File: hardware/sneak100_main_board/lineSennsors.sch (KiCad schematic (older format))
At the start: 4 parts, among them J1 Conn_01x03, J2 Conn_01x03, J3 Conn_01x03, J4 Conn_01x03

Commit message: Proximity sensor first test
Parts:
- renumbered J1 to J2, J2 to J3, J3 to J4, J4 to J5
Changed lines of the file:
@@
 $EndDescr
 $Comp
-L Connector_Generic:Conn_01x03 J1
+L Connector_Generic:Conn_01x03 J2
 U 1 1 60E05377
 P 4050 2550
-F 0 "J1" H 4130 2592 50  0000 L CNN
+F 0 "J2" H 4130 2592 50  0000 L CNN
 F 1 "Conn_01x03" H 4130 2501 50  0000 L CNN
 F 2 "" H 4050 2550 50  0001 C CNN
@@
 $EndComp
 $Comp
-L Connector_Generic:Conn_01x03 J2
+L Connector_Generic:Conn_01x03 J3
 U 1 1 60E06B30
 P 4050 2950
-F 0 "J2" H 4130 2992 50  0000 L CNN
+F 0 "J3" H 4130 2992 50  0000 L CNN
 F 1 "Conn_01x03" H 4130 2901 50  0000 L CNN
 F 2 "" H 4050 2950 50  0001 C CNN
@@
 $EndComp
 $Comp
-L Connector_Generic:Conn_01x03 J3
+L Connector_Generic:Conn_01x03 J4
 U 1 1 60E07495
 P 4050 3350
-F 0 "J3" H 4130 3392 50  0000 L CNN
+F 0 "J4" H 4130 3392 50  0000 L CNN
 F 1 "Conn_01x03" H 4130 3301 50  0000 L CNN
 F 2 "" H 4050 3350 50  0001 C CNN
@@
 $EndComp
 $Comp
-L Connector_Generic:Conn_01x03 J4
+L Connector_Generic:Conn_01x03 J5
 U 1 1 60E07950
 P 4050 3750
-F 0 "J4" H 4130 3792 50  0000 L CNN
+F 0 "J5" H 4130 3792 50  0000 L CNN
 F 1 "Conn_01x03" H 4130 3701 50  0000 L CNN
 F 2 "" H 4050 3750 50  0001 C CNN
@@
 $EndComp
 $Comp
-L power:+3.3V #PWR0101
+L power:+3.3V #PWR040
 U 1 1 60E08D03
 P 3850 2550
-F 0 "#PWR0101" H 3850 2400 50  0001 C CNN
+F 0 "#PWR040" H 3850 2400 50  0001 C CNN
 F 1 "+3.3V" V 3865 2678 50  0000 L CNN
 F 2 "" H 3850 2550 50  0001 C CNN
@@
 $EndComp
 $Comp
-L power:+3.3V #PWR0102
+L power:+3.3V #PWR042
 U 1 1 60E097F5
 P 3850 2950
-F 0 "#PWR0102" H 3850 2800 50  0001 C CNN
+F 0 "#PWR042" H 3850 2800 50  0001 C CNN
 F 1 "+3.3V" V 3865 3078 50  0000 L CNN
 F 2 "" H 3850 2950 50  0001 C CNN
@@
 $EndComp
 $Comp
-L power:+3.3V #PWR0103
+L power:+3.3V #PWR044
 U 1 1 60E09BF6
 P 3850 3350
-F 0 "#PWR0103" H 3850 3200 50  0001 C CNN
+F 0 "#PWR044" H 3850 3200 50  0001 C CNN
 F 1 "+3.3V" V 3865 3478 50  0000 L CNN
 F 2 "" H 3850 3350 50  0001 C CNN
@@
 $EndComp
 $Comp
-L power:+3.3V #PWR0104
+L power:+3.3V #PWR046
 U 1 1 60E0A09F
 P 3850 3750
-F 0 "#PWR0104" H 3850 3600 50  0001 C CNN
+F 0 "#PWR046" H 3850 3600 50  0001 C CNN
 F 1 "+3.3V" V 3865 3878 50  0000 L CNN
 F 2 "" H 3850 3750 50  0001 C CNN
@@
 $EndComp
 $Comp
-L power:GND #PWR0105
+L power:GND #PWR047
 U 1 1 60E0A641
 P 3850 3850
-F 0 "#PWR0105" H 3850 3600 50  0001 C CNN
+F 0 "#PWR047" H 3850 3600 50  0001 C CNN
 F 1 "GND" V 3855 3722 50  0000 R CNN
 F 2 "" H 3850 3850 50  0001 C CNN
@@
 $EndComp
 $Comp
-L power:GND #PWR0106
+L power:GND #PWR045
 U 1 1 60E0ADFF
 P 3850 3450
-F 0 "#PWR0106" H 3850 3200 50  0001 C CNN
+F 0 "#PWR045" H 3850 3200 50  0001 C CNN
 F 1 "GND" V 3855 3322 50  0000 R CNN
 F 2 "" H 3850 3450 50  0001 C CNN
@@
 $EndComp
 $Comp
-L power:GND #PWR0107
+L power:GND #PWR043
 U 1 1 60E0B1BF
 P 3850 3050
-F 0 "#PWR0107" H 3850 2800 50  0001 C CNN
+F 0 "#PWR043" H 3850 2800 50  0001 C CNN
 F 1 "GND" V 3855 2922 50  0000 R CNN
 F 2 "" H 3850 3050 50  0001 C CNN
@@
 $EndComp
 $Comp
-L power:GND #PWR0108
+L power:GND #PWR041
 U 1 1 60E0B57F
 P 3850 2650
-F 0 "#PWR0108" H 3850 2400 50  0001 C CNN
+F 0 "#PWR041" H 3850 2400 50  0001 C CNN
 F 1 "GND" V 3855 2522 50  0000 R CNN
 F 2 "" H 3850 2650 50  0001 C CNN

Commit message: motors circuit scheme
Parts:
- J10: renamed from J5; footprint (none) -> Connector_PinHeader_2.54mm:PinHeader_1x03_P2.54mm_Vertical
- J7: renamed from J2; footprint (none) -> Connector_PinHeader_2.54mm:PinHeader_1x03_P2.54mm_Vertical
- J8: renamed from J3; footprint (none) -> Connector_PinHeader_2.54mm:PinHeader_1x03_P2.54mm_Vertical
- J9: renamed from J4; footprint (none) -> Connector_PinHeader_2.54mm:PinHeader_1x03_P2.54mm_Vertical
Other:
- note added: "QTR-1A sensors connection"
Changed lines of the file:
@@
 $EndDescr
 $Comp
-L Connector_Generic:Conn_01x03 J2
+L Connector_Generic:Conn_01x03 J7
 U 1 1 60E05377
 P 4050 2550
-F 0 "J2" H 4130 2592 50  0000 L CNN
+F 0 "J7" H 4130 2592 50  0000 L CNN
 F 1 "Conn_01x03" H 4130 2501 50  0000 L CNN
-F 2 "" H 4050 2550 50  0001 C CNN
+F 2 "Connector_PinHeader_2.54mm:PinHeader_1x03_P2.54mm_Vertical" H 4050 2550 50  0001 C CNN
 F 3 "~" H 4050 2550 50  0001 C CNN
 	1    4050 2550
@@
 $EndComp
 $Comp
-L Connector_Generic:Conn_01x03 J3
+L Connector_Generic:Conn_01x03 J8
 U 1 1 60E06B30
 P 4050 2950
-F 0 "J3" H 4130 2992 50  0000 L CNN
+F 0 "J8" H 4130 2992 50  0000 L CNN
 F 1 "Conn_01x03" H 4130 2901 50  0000 L CNN
-F 2 "" H 4050 2950 50  0001 C CNN
+F 2 "Connector_PinHeader_2.54mm:PinHeader_1x03_P2.54mm_Vertical" H 4050 2950 50  0001 C CNN
 F 3 "~" H 4050 2950 50  0001 C CNN
 	1    4050 2950
@@
 $EndComp
 $Comp
-L Connector_Generic:Conn_01x03 J4
+L Connector_Generic:Conn_01x03 J9
 U 1 1 60E07495
 P 4050 3350
-F 0 "J4" H 4130 3392 50  0000 L CNN
+F 0 "J9" H 4130 3392 50  0000 L CNN
 F 1 "Conn_01x03" H 4130 3301 50  0000 L CNN
-F 2 "" H 4050 3350 50  0001 C CNN
+F 2 "Connector_PinHeader_2.54mm:PinHeader_1x03_P2.54mm_Vertical" H 4050 3350 50  0001 C CNN
 F 3 "~" H 4050 3350 50  0001 C CNN
 	1    4050 3350
@@
 $EndComp
 $Comp
-L Connector_Generic:Conn_01x03 J5
+L Connector_Generic:Conn_01x03 J10
 U 1 1 60E07950
 P 4050 3750
-F 0 "J5" H 4130 3792 50  0000 L CNN
+F 0 "J10" H 4130 3792 50  0000 L CNN
 F 1 "Conn_01x03" H 4130 3701 50  0000 L CNN
-F 2 "" H 4050 3750 50  0001 C CNN
+F 2 "Connector_PinHeader_2.54mm:PinHeader_1x03_P2.54mm_Vertical" H 4050 3750 50  0001 C CNN
 F 3 "~" H 4050 3750 50  0001 C CNN
 	1    4050 3750
@@
 $EndComp
 $Comp
-L power:+3.3V #PWR040
+L power:+3.3V #PWR072
 U 1 1 60E08D03
 P 3850 2550
-F 0 "#PWR040" H 3850 2400 50  0001 C CNN
+F 0 "#PWR072" H 3850 2400 50  0001 C CNN
 F 1 "+3.3V" V 3865 2678 50  0000 L CNN
 F 2 "" H 3850 2550 50  0001 C CNN
@@
 $EndComp
 $Comp
-L power:+3.3V #PWR042
+L power:+3.3V #PWR074
 U 1 1 60E097F5
 P 3850 2950
-F 0 "#PWR042" H 3850 2800 50  0001 C CNN
+F 0 "#PWR074" H 3850 2800 50  0001 C CNN
 F 1 "+3.3V" V 3865 3078 50  0000 L CNN
 F 2 "" H 3850 2950 50  0001 C CNN
@@
 $EndComp
 $Comp
-L power:+3.3V #PWR044
+L power:+3.3V #PWR076
 U 1 1 60E09BF6
 P 3850 3350
-F 0 "#PWR044" H 3850 3200 50  0001 C CNN
+F 0 "#PWR076" H 3850 3200 50  0001 C CNN
 F 1 "+3.3V" V 3865 3478 50  0000 L CNN
 F 2 "" H 3850 3350 50  0001 C CNN
@@
 $EndComp
 $Comp
-L power:+3.3V #PWR046
+L power:+3.3V #PWR078
 U 1 1 60E0A09F
 P 3850 3750
-F 0 "#PWR046" H 3850 3600 50  0001 C CNN
+F 0 "#PWR078" H 3850 3600 50  0001 C CNN
 F 1 "+3.3V" V 3865 3878 50  0000 L CNN
 F 2 "" H 3850 3750 50  0001 C CNN
@@
 $EndComp
 $Comp
-L power:GND #PWR047
+L power:GND #PWR079
 U 1 1 60E0A641
 P 3850 3850
-F 0 "#PWR047" H 3850 3600 50  0001 C CNN
+F 0 "#PWR079" H 3850 3600 50  0001 C CNN
 F 1 "GND" V 3855 3722 50  0000 R CNN
 F 2 "" H 3850 3850 50  0001 C CNN
@@
 $EndComp
 $Comp
-L power:GND #PWR045
+L power:GND #PWR077
 U 1 1 60E0ADFF
 P 3850 3450
-F 0 "#PWR045" H 3850 3200 50  0001 C CNN
+F 0 "#PWR077" H 3850 3200 50  0001 C CNN
 F 1 "GND" V 3855 3322 50  0000 R CNN
 F 2 "" H 3850 3450 50  0001 C CNN
@@
 $EndComp
 $Comp
-L power:GND #PWR043
+L power:GND #PWR075
 U 1 1 60E0B1BF
 P 3850 3050
-F 0 "#PWR043" H 3850 2800 50  0001 C CNN
+F 0 "#PWR075" H 3850 2800 50  0001 C CNN
 F 1 "GND" V 3855 2922 50  0000 R CNN
 F 2 "" H 3850 3050 50  0001 C CNN
@@
 $EndComp
 $Comp
-L power:GND #PWR041
+L power:GND #PWR073
 U 1 1 60E0B57F
 P 3850 2650
-F 0 "#PWR041" H 3850 2400 50  0001 C CNN
+F 0 "#PWR073" H 3850 2400 50  0001 C CNN
 F 1 "GND" V 3855 2522 50  0000 R CNN
 F 2 "" H 3850 2650 50  0001 C CNN
@@
 Text HLabel 3850 3650 0    50   Output ~ 0
 READ_RR
+Text Notes 2950 2150 0    100  ~ 20
+QTR-1A sensors connection
 $EndSCHEMATC

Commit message: Add stm32f405 uC scheme
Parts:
- renumbered J7 to J6, J8 to J7, J9 to J8, J10 to J9
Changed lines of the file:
@@
 $EndDescr
 $Comp
-L Connector_Generic:Conn_01x03 J7
+L Connector_Generic:Conn_01x03 J6
 U 1 1 60E05377
 P 4050 2550
-F 0 "J7" H 4130 2592 50  0000 L CNN
+F 0 "J6" H 4130 2592 50  0000 L CNN
 F 1 "Conn_01x03" H 4130 2501 50  0000 L CNN
 F 2 "Connector_PinHeader_2.54mm:PinHeader_1x03_P2.54mm_Vertical" H 4050 2550 50  0001 C CNN
@@
 $EndComp
 $Comp
-L Connector_Generic:Conn_01x03 J8
+L Connector_Generic:Conn_01x03 J7
 U 1 1 60E06B30
 P 4050 2950
-F 0 "J8" H 4130 2992 50  0000 L CNN
+F 0 "J7" H 4130 2992 50  0000 L CNN
 F 1 "Conn_01x03" H 4130 2901 50  0000 L CNN
 F 2 "Connector_PinHeader_2.54mm:PinHeader_1x03_P2.54mm_Vertical" H 4050 2950 50  0001 C CNN
@@
 $EndComp
 $Comp
-L Connector_Generic:Conn_01x03 J9
+L Connector_Generic:Conn_01x03 J8
 U 1 1 60E07495
 P 4050 3350
-F 0 "J9" H 4130 3392 50  0000 L CNN
+F 0 "J8" H 4130 3392 50  0000 L CNN
 F 1 "Conn_01x03" H 4130 3301 50  0000 L CNN
 F 2 "Connector_PinHeader_2.54mm:PinHeader_1x03_P2.54mm_Vertical" H 4050 3350 50  0001 C CNN
@@
 $EndComp
 $Comp
-L Connector_Generic:Conn_01x03 J10
+L Connector_Generic:Conn_01x03 J9
 U 1 1 60E07950
 P 4050 3750
-F 0 "J10" H 4130 3792 50  0000 L CNN
+F 0 "J9" H 4130 3792 50  0000 L CNN
 F 1 "Conn_01x03" H 4130 3701 50  0000 L CNN
 F 2 "Connector_PinHeader_2.54mm:PinHeader_1x03_P2.54mm_Vertical" H 4050 3750 50  0001 C CNN

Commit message: Hardware configuration schematic
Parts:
- renumbered J7 to J10, J8 to J11, J9 to J12, J6 to J9
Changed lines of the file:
@@
 $Descr A4 11693 8268
 encoding utf-8
-Sheet 7 7
+Sheet 6 7
 Title ""
 Date ""
@@
 $EndDescr
 $Comp
-L Connector_Generic:Conn_01x03 J6
+L Connector_Generic:Conn_01x03 J9
 U 1 1 60E05377
 P 4050 2550
-F 0 "J6" H 4130 2592 50  0000 L CNN
+F 0 "J9" H 4130 2592 50  0000 L CNN
 F 1 "Conn_01x03" H 4130 2501 50  0000 L CNN
 F 2 "Connector_PinHeader_2.54mm:PinHeader_1x03_P2.54mm_Vertical" H 4050 2550 50  0001 C CNN
@@
 $EndComp
 $Comp
-L Connector_Generic:Conn_01x03 J7
+L Connector_Generic:Conn_01x03 J10
 U 1 1 60E06B30
 P 4050 2950
-F 0 "J7" H 4130 2992 50  0000 L CNN
+F 0 "J10" H 4130 2992 50  0000 L CNN
 F 1 "Conn_01x03" H 4130 2901 50  0000 L CNN
 F 2 "Connector_PinHeader_2.54mm:PinHeader_1x03_P2.54mm_Vertical" H 4050 2950 50  0001 C CNN
@@
 $EndComp
 $Comp
-L Connector_Generic:Conn_01x03 J8
+L Connector_Generic:Conn_01x03 J11
 U 1 1 60E07495
 P 4050 3350
-F 0 "J8" H 4130 3392 50  0000 L CNN
+F 0 "J11" H 4130 3392 50  0000 L CNN
 F 1 "Conn_01x03" H 4130 3301 50  0000 L CNN
 F 2 "Connector_PinHeader_2.54mm:PinHeader_1x03_P2.54mm_Vertical" H 4050 3350 50  0001 C CNN
@@
 $EndComp
 $Comp
-L Connector_Generic:Conn_01x03 J9
+L Connector_Generic:Conn_01x03 J12
 U 1 1 60E07950
 P 4050 3750
-F 0 "J9" H 4130 3792 50  0000 L CNN
+F 0 "J12" H 4130 3792 50  0000 L CNN
 F 1 "Conn_01x03" H 4130 3701 50  0000 L CNN
 F 2 "Connector_PinHeader_2.54mm:PinHeader_1x03_P2.54mm_Vertical" H 4050 3750 50  0001 C CNN
@@
 $EndComp
 $Comp
-L power:+3.3V #PWR072
+L power:+3.3V #PWR081
 U 1 1 60E08D03
 P 3850 2550
-F 0 "#PWR072" H 3850 2400 50  0001 C CNN
+F 0 "#PWR081" H 3850 2400 50  0001 C CNN
 F 1 "+3.3V" V 3865 2678 50  0000 L CNN
 F 2 "" H 3850 2550 50  0001 C CNN
@@
 $EndComp
 $Comp
-L power:+3.3V #PWR074
+L power:+3.3V #PWR083
 U 1 1 60E097F5
 P 3850 2950
-F 0 "#PWR074" H 3850 2800 50  0001 C CNN
+F 0 "#PWR083" H 3850 2800 50  0001 C CNN
 F 1 "+3.3V" V 3865 3078 50  0000 L CNN
 F 2 "" H 3850 2950 50  0001 C CNN
@@
 $EndComp
 $Comp
-L power:+3.3V #PWR076
+L power:+3.3V #PWR085
 U 1 1 60E09BF6
 P 3850 3350
-F 0 "#PWR076" H 3850 3200 50  0001 C CNN
+F 0 "#PWR085" H 3850 3200 50  0001 C CNN
 F 1 "+3.3V" V 3865 3478 50  0000 L CNN
 F 2 "" H 3850 3350 50  0001 C CNN
@@
 $EndComp
 $Comp
-L power:+3.3V #PWR078
+L power:+3.3V #PWR087
 U 1 1 60E0A09F
 P 3850 3750
-F 0 "#PWR078" H 3850 3600 50  0001 C CNN
+F 0 "#PWR087" H 3850 3600 50  0001 C CNN
 F 1 "+3.3V" V 3865 3878 50  0000 L CNN
 F 2 "" H 3850 3750 50  0001 C CNN
@@
 $EndComp
 $Comp
-L power:GND #PWR079
+L power:GND #PWR088
 U 1 1 60E0A641
 P 3850 3850
-F 0 "#PWR079" H 3850 3600 50  0001 C CNN
+F 0 "#PWR088" H 3850 3600 50  0001 C CNN
 F 1 "GND" V 3855 3722 50  0000 R CNN
 F 2 "" H 3850 3850 50  0001 C CNN
@@
 $EndComp
 $Comp
-L power:GND #PWR077
+L power:GND #PWR086
 U 1 1 60E0ADFF
 P 3850 3450
-F 0 "#PWR077" H 3850 3200 50  0001 C CNN
+F 0 "#PWR086" H 3850 3200 50  0001 C CNN
 F 1 "GND" V 3855 3322 50  0000 R CNN
 F 2 "" H 3850 3450 50  0001 C CNN
@@
 $EndComp
 $Comp
-L power:GND #PWR075
+L power:GND #PWR084
 U 1 1 60E0B1BF
 P 3850 3050
-F 0 "#PWR075" H 3850 2800 50  0001 C CNN
+F 0 "#PWR084" H 3850 2800 50  0001 C CNN
 F 1 "GND" V 3855 2922 50  0000 R CNN
 F 2 "" H 3850 3050 50  0001 C CNN
@@
 $EndComp
 $Comp
-L power:GND #PWR073
+L power:GND #PWR082
 U 1 1 60E0B57F
 P 3850 2650
-F 0 "#PWR073" H 3850 2400 50  0001 C CNN
+F 0 "#PWR082" H 3850 2400 50  0001 C CNN
 F 1 "GND" V 3855 2522 50  0000 R CNN
 F 2 "" H 3850 2650 50  0001 C CNN

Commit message: Power section scheme
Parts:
- renumbered J9 to J11, J10 to J12, J11 to J13, J12 to J14
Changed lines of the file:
@@
 $EndDescr
 $Comp
-L Connector_Generic:Conn_01x03 J9
+L Connector_Generic:Conn_01x03 J11
 U 1 1 60E05377
 P 4050 2550
-F 0 "J9" H 4130 2592 50  0000 L CNN
+F 0 "J11" H 4130 2592 50  0000 L CNN
 F 1 "Conn_01x03" H 4130 2501 50  0000 L CNN
 F 2 "Connector_PinHeader_2.54mm:PinHeader_1x03_P2.54mm_Vertical" H 4050 2550 50  0001 C CNN
@@
 $EndComp
 $Comp
-L Connector_Generic:Conn_01x03 J10
+L Connector_Generic:Conn_01x03 J12
 U 1 1 60E06B30
 P 4050 2950
-F 0 "J10" H 4130 2992 50  0000 L CNN
+F 0 "J12" H 4130 2992 50  0000 L CNN
 F 1 "Conn_01x03" H 4130 2901 50  0000 L CNN
 F 2 "Connector_PinHeader_2.54mm:PinHeader_1x03_P2.54mm_Vertical" H 4050 2950 50  0001 C CNN
@@
 $EndComp
 $Comp
-L Connector_Generic:Conn_01x03 J11
+L Connector_Generic:Conn_01x03 J13
 U 1 1 60E07495
 P 4050 3350
-F 0 "J11" H 4130 3392 50  0000 L CNN
+F 0 "J13" H 4130 3392 50  0000 L CNN
 F 1 "Conn_01x03" H 4130 3301 50  0000 L CNN
 F 2 "Connector_PinHeader_2.54mm:PinHeader_1x03_P2.54mm_Vertical" H 4050 3350 50  0001 C CNN
@@
 $EndComp
 $Comp
-L Connector_Generic:Conn_01x03 J12
+L Connector_Generic:Conn_01x03 J14
 U 1 1 60E07950
 P 4050 3750
-F 0 "J12" H 4130 3792 50  0000 L CNN
+F 0 "J14" H 4130 3792 50  0000 L CNN
 F 1 "Conn_01x03" H 4130 3701 50  0000 L CNN
 F 2 "Connector_PinHeader_2.54mm:PinHeader_1x03_P2.54mm_Vertical" H 4050 3750 50  0001 C CNN
@@
 $EndComp
 $Comp
-L power:+3.3V #PWR081
+L power:+3.3V #PWR0101
 U 1 1 60E08D03
 P 3850 2550
-F 0 "#PWR081" H 3850 2400 50  0001 C CNN
+F 0 "#PWR0101" H 3850 2400 50  0001 C CNN
 F 1 "+3.3V" V 3865 2678 50  0000 L CNN
 F 2 "" H 3850 2550 50  0001 C CNN
@@
 $EndComp
 $Comp
-L power:+3.3V #PWR083
+L power:+3.3V #PWR0103
 U 1 1 60E097F5
 P 3850 2950
-F 0 "#PWR083" H 3850 2800 50  0001 C CNN
+F 0 "#PWR0103" H 3850 2800 50  0001 C CNN
 F 1 "+3.3V" V 3865 3078 50  0000 L CNN
 F 2 "" H 3850 2950 50  0001 C CNN
@@
 $EndComp
 $Comp
-L power:+3.3V #PWR085
+L power:+3.3V #PWR0105
 U 1 1 60E09BF6
 P 3850 3350
-F 0 "#PWR085" H 3850 3200 50  0001 C CNN
+F 0 "#PWR0105" H 3850 3200 50  0001 C CNN
 F 1 "+3.3V" V 3865 3478 50  0000 L CNN
 F 2 "" H 3850 3350 50  0001 C CNN
@@
 $EndComp
 $Comp
-L power:+3.3V #PWR087
+L power:+3.3V #PWR0107
 U 1 1 60E0A09F
 P 3850 3750
-F 0 "#PWR087" H 3850 3600 50  0001 C CNN
+F 0 "#PWR0107" H 3850 3600 50  0001 C CNN
 F 1 "+3.3V" V 3865 3878 50  0000 L CNN
 F 2 "" H 3850 3750 50  0001 C CNN
@@
 $EndComp
 $Comp
-L power:GND #PWR088
+L power:GND #PWR0108
 U 1 1 60E0A641
 P 3850 3850
-F 0 "#PWR088" H 3850 3600 50  0001 C CNN
+F 0 "#PWR0108" H 3850 3600 50  0001 C CNN
 F 1 "GND" V 3855 3722 50  0000 R CNN
 F 2 "" H 3850 3850 50  0001 C CNN
@@
 $EndComp
 $Comp
-L power:GND #PWR086
+L power:GND #PWR0106
 U 1 1 60E0ADFF
 P 3850 3450
-F 0 "#PWR086" H 3850 3200 50  0001 C CNN
+F 0 "#PWR0106" H 3850 3200 50  0001 C CNN
 F 1 "GND" V 3855 3322 50  0000 R CNN
 F 2 "" H 3850 3450 50  0001 C CNN
@@
 $EndComp
 $Comp
-L power:GND #PWR084
+L power:GND #PWR0104
 U 1 1 60E0B1BF
 P 3850 3050
-F 0 "#PWR084" H 3850 2800 50  0001 C CNN
+F 0 "#PWR0104" H 3850 2800 50  0001 C CNN
 F 1 "GND" V 3855 2922 50  0000 R CNN
 F 2 "" H 3850 3050 50  0001 C CNN
@@
 $EndComp
 $Comp
-L power:GND #PWR082
+L power:GND #PWR0102
 U 1 1 60E0B57F
 P 3850 2650
-F 0 "#PWR082" H 3850 2400 50  0001 C CNN
+F 0 "#PWR0102" H 3850 2400 50  0001 C CNN
 F 1 "GND" V 3855 2522 50  0000 R CNN
 F 2 "" H 3850 2650 50  0001 C CNN

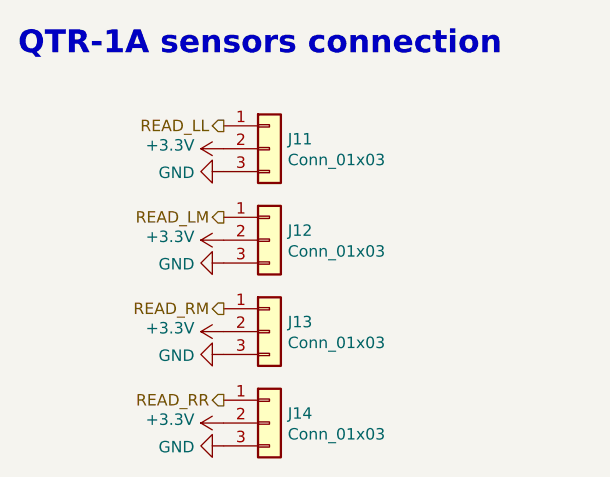
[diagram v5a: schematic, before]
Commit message: USB FDU mode
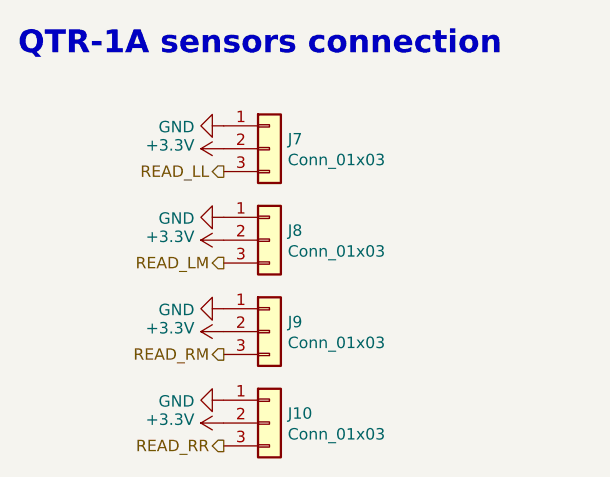
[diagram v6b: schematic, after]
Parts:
- renumbered J14 to J10, J11 to J7, J12 to J8, J13 to J9
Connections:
- net GND: now also J10.1 (Pin_1), J7.1 (Pin_1), J8.1 (Pin_1), J9.1 (Pin_1); no longer J10.3 (Pin_3), J7.3 (Pin_3), J8.3 (Pin_3), J9.3 (Pin_3)
- net READ_LL: now also J7.3 (Pin_3); no longer J7.1 (Pin_1)
- net READ_LM: now also J8.3 (Pin_3); no longer J8.1 (Pin_1)
- net READ_RM: now also J9.3 (Pin_3); no longer J9.1 (Pin_1)
- net READ_RR: now also J10.3 (Pin_3); no longer J10.1 (Pin_1)
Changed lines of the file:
@@
 $Descr A4 11693 8268
 encoding utf-8
-Sheet 6 7
+Sheet 5 7
 Title ""
 Date ""
@@
 $EndDescr
 $Comp
-L Connector_Generic:Conn_01x03 J11
+L Connector_Generic:Conn_01x03 J7
 U 1 1 60E05377
 P 4050 2550
-F 0 "J11" H 4130 2592 50  0000 L CNN
+F 0 "J7" H 4130 2592 50  0000 L CNN
 F 1 "Conn_01x03" H 4130 2501 50  0000 L CNN
 F 2 "Connector_PinHeader_2.54mm:PinHeader_1x03_P2.54mm_Vertical" H 4050 2550 50  0001 C CNN
@@
 $EndComp
 $Comp
-L Connector_Generic:Conn_01x03 J12
+L Connector_Generic:Conn_01x03 J8
 U 1 1 60E06B30
 P 4050 2950
-F 0 "J12" H 4130 2992 50  0000 L CNN
+F 0 "J8" H 4130 2992 50  0000 L CNN
 F 1 "Conn_01x03" H 4130 2901 50  0000 L CNN
 F 2 "Connector_PinHeader_2.54mm:PinHeader_1x03_P2.54mm_Vertical" H 4050 2950 50  0001 C CNN
@@
 $EndComp
 $Comp
-L Connector_Generic:Conn_01x03 J13
+L Connector_Generic:Conn_01x03 J9
 U 1 1 60E07495
 P 4050 3350
-F 0 "J13" H 4130 3392 50  0000 L CNN
+F 0 "J9" H 4130 3392 50  0000 L CNN
 F 1 "Conn_01x03" H 4130 3301 50  0000 L CNN
 F 2 "Connector_PinHeader_2.54mm:PinHeader_1x03_P2.54mm_Vertical" H 4050 3350 50  0001 C CNN
@@
 $EndComp
 $Comp
-L Connector_Generic:Conn_01x03 J14
+L Connector_Generic:Conn_01x03 J10
 U 1 1 60E07950
 P 4050 3750
-F 0 "J14" H 4130 3792 50  0000 L CNN
+F 0 "J10" H 4130 3792 50  0000 L CNN
 F 1 "Conn_01x03" H 4130 3701 50  0000 L CNN
 F 2 "Connector_PinHeader_2.54mm:PinHeader_1x03_P2.54mm_Vertical" H 4050 3750 50  0001 C CNN
@@
 $EndComp
 $Comp
-L power:+3.3V #PWR0101
+L power:+3.3V #PWR078
 U 1 1 60E08D03
 P 3850 2550
-F 0 "#PWR0101" H 3850 2400 50  0001 C CNN
+F 0 "#PWR078" H 3850 2400 50  0001 C CNN
 F 1 "+3.3V" V 3865 2678 50  0000 L CNN
 F 2 "" H 3850 2550 50  0001 C CNN
@@
 $EndComp
 $Comp
-L power:+3.3V #PWR0103
+L power:+3.3V #PWR080
 U 1 1 60E097F5
 P 3850 2950
-F 0 "#PWR0103" H 3850 2800 50  0001 C CNN
+F 0 "#PWR080" H 3850 2800 50  0001 C CNN
 F 1 "+3.3V" V 3865 3078 50  0000 L CNN
 F 2 "" H 3850 2950 50  0001 C CNN
@@
 $EndComp
 $Comp
-L power:+3.3V #PWR0105
+L power:+3.3V #PWR082
 U 1 1 60E09BF6
 P 3850 3350
-F 0 "#PWR0105" H 3850 3200 50  0001 C CNN
+F 0 "#PWR082" H 3850 3200 50  0001 C CNN
 F 1 "+3.3V" V 3865 3478 50  0000 L CNN
 F 2 "" H 3850 3350 50  0001 C CNN
@@
 $EndComp
 $Comp
-L power:+3.3V #PWR0107
+L power:+3.3V #PWR084
 U 1 1 60E0A09F
 P 3850 3750
-F 0 "#PWR0107" H 3850 3600 50  0001 C CNN
+F 0 "#PWR084" H 3850 3600 50  0001 C CNN
 F 1 "+3.3V" V 3865 3878 50  0000 L CNN
 F 2 "" H 3850 3750 50  0001 C CNN
@@
 $EndComp
 $Comp
-L power:GND #PWR0108
+L power:GND #PWR083
 U 1 1 60E0A641
-P 3850 3850
-F 0 "#PWR0108" H 3850 3600 50  0001 C CNN
-F 1 "GND" V 3855 3722 50  0000 R CNN
-F 2 "" H 3850 3850 50  0001 C CNN
-F 3 "" H 3850 3850 50  0001 C CNN
-	1    3850 3850
+P 3850 3650
+F 0 "#PWR083" H 3850 3400 50  0001 C CNN
+F 1 "GND" V 3855 3522 50  0000 R CNN
+F 2 "" H 3850 3650 50  0001 C CNN
+F 3 "" H 3850 3650 50  0001 C CNN
+	1    3850 3650
 	0    1    1    0
 $EndComp
 $Comp
-L power:GND #PWR0106
+L power:GND #PWR081
 U 1 1 60E0ADFF
-P 3850 3450
-F 0 "#PWR0106" H 3850 3200 50  0001 C CNN
-F 1 "GND" V 3855 3322 50  0000 R CNN
-F 2 "" H 3850 3450 50  0001 C CNN
-F 3 "" H 3850 3450 50  0001 C CNN
-	1    3850 3450
+P 3850 3250
+F 0 "#PWR081" H 3850 3000 50  0001 C CNN
+F 1 "GND" V 3855 3122 50  0000 R CNN
+F 2 "" H 3850 3250 50  0001 C CNN
+F 3 "" H 3850 3250 50  0001 C CNN
+	1    3850 3250
 	0    1    1    0
 $EndComp
 $Comp
-L power:GND #PWR0104
+L power:GND #PWR079
 U 1 1 60E0B1BF
-P 3850 3050
-F 0 "#PWR0104" H 3850 2800 50  0001 C CNN
-F 1 "GND" V 3855 2922 50  0000 R CNN
-F 2 "" H 3850 3050 50  0001 C CNN
-F 3 "" H 3850 3050 50  0001 C CNN
-	1    3850 3050
+P 3850 2850
+F 0 "#PWR079" H 3850 2600 50  0001 C CNN
+F 1 "GND" V 3855 2722 50  0000 R CNN
+F 2 "" H 3850 2850 50  0001 C CNN
+F 3 "" H 3850 2850 50  0001 C CNN
+	1    3850 2850
 	0    1    1    0
 $EndComp
 $Comp
-L power:GND #PWR0102
+L power:GND #PWR077
 U 1 1 60E0B57F
-P 3850 2650
-F 0 "#PWR0102" H 3850 2400 50  0001 C CNN
-F 1 "GND" V 3855 2522 50  0000 R CNN
-F 2 "" H 3850 2650 50  0001 C CNN
-F 3 "" H 3850 2650 50  0001 C CNN
-	1    3850 2650
+P 3850 2450
+F 0 "#PWR077" H 3850 2200 50  0001 C CNN
+F 1 "GND" V 3855 2322 50  0000 R CNN
+F 2 "" H 3850 2450 50  0001 C CNN
+F 3 "" H 3850 2450 50  0001 C CNN
+	1    3850 2450
 	0    1    1    0
 $EndComp
-Text HLabel 3850 2450 0    50   Output ~ 0
+Text HLabel 3850 2650 0    50   Output ~ 0
 READ_LL
-Text HLabel 3850 2850 0    50   Output ~ 0
+Text HLabel 3850 3050 0    50   Output ~ 0
 READ_LM
-Text HLabel 3850 3250 0    50   Output ~ 0
+Text HLabel 3850 3450 0    50   Output ~ 0
 READ_RM
-Text HLabel 3850 3650 0    50   Output ~ 0
+Text HLabel 3850 3850 0    50   Output ~ 0
 READ_RR
 Text Notes 2950 2150 0    100  ~ 20
